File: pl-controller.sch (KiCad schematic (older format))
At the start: 31 parts

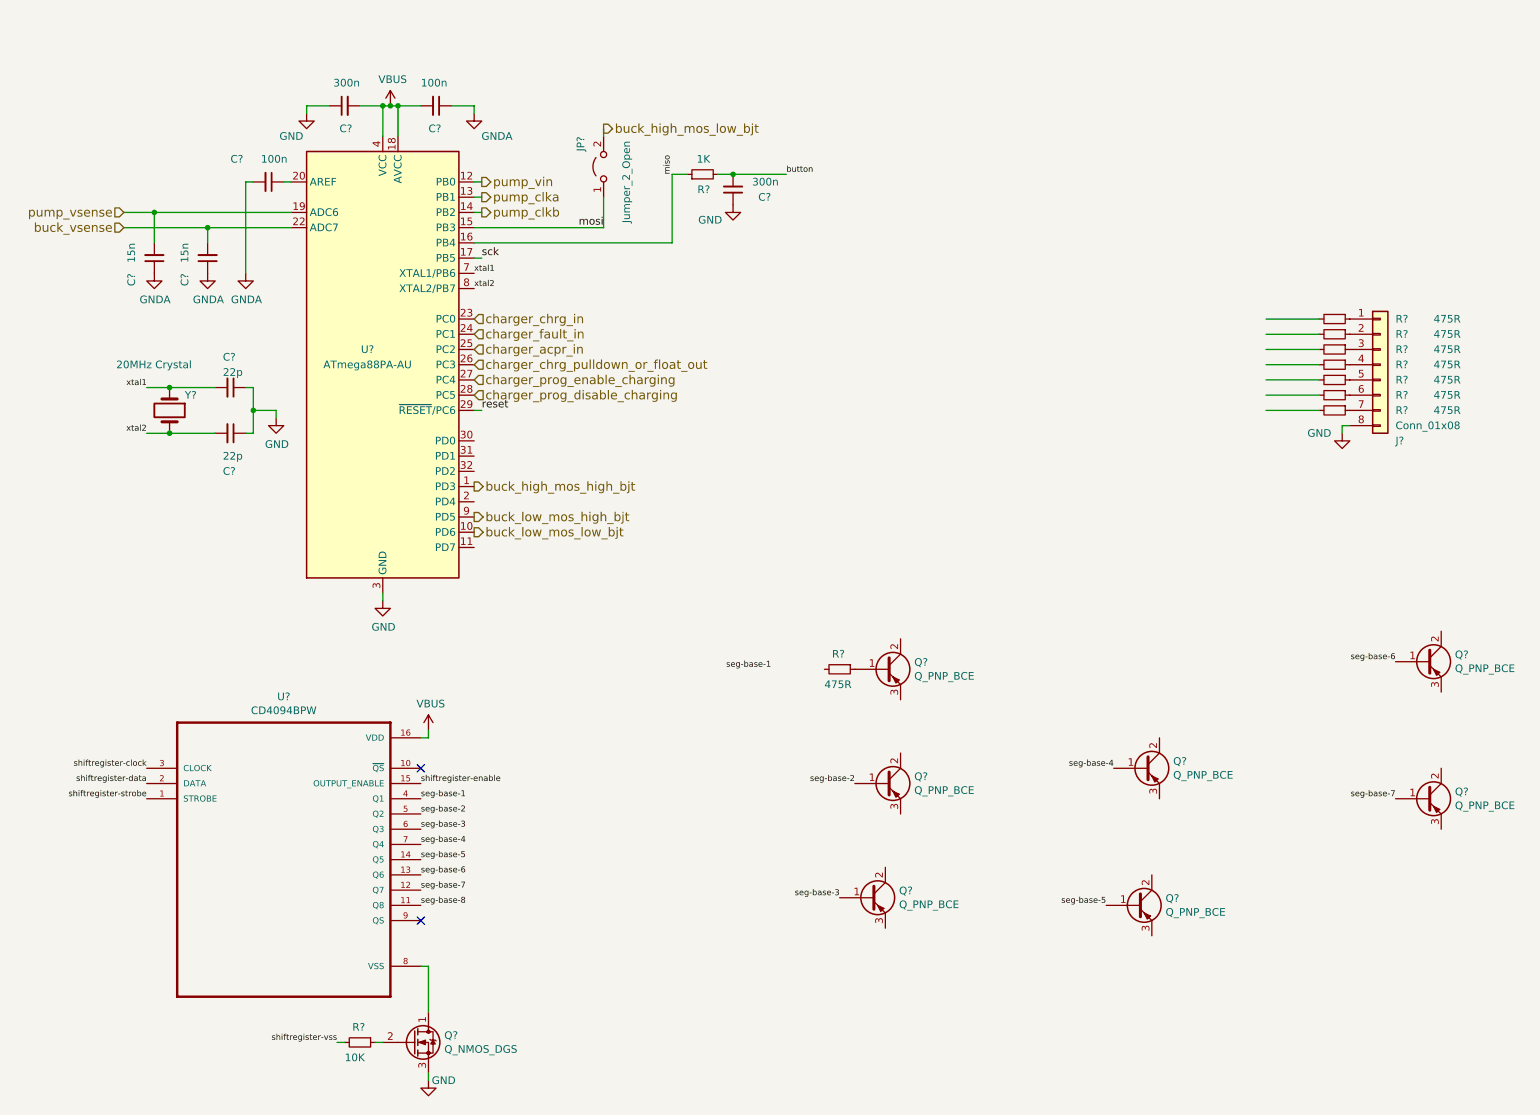
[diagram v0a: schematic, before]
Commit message: Added component values
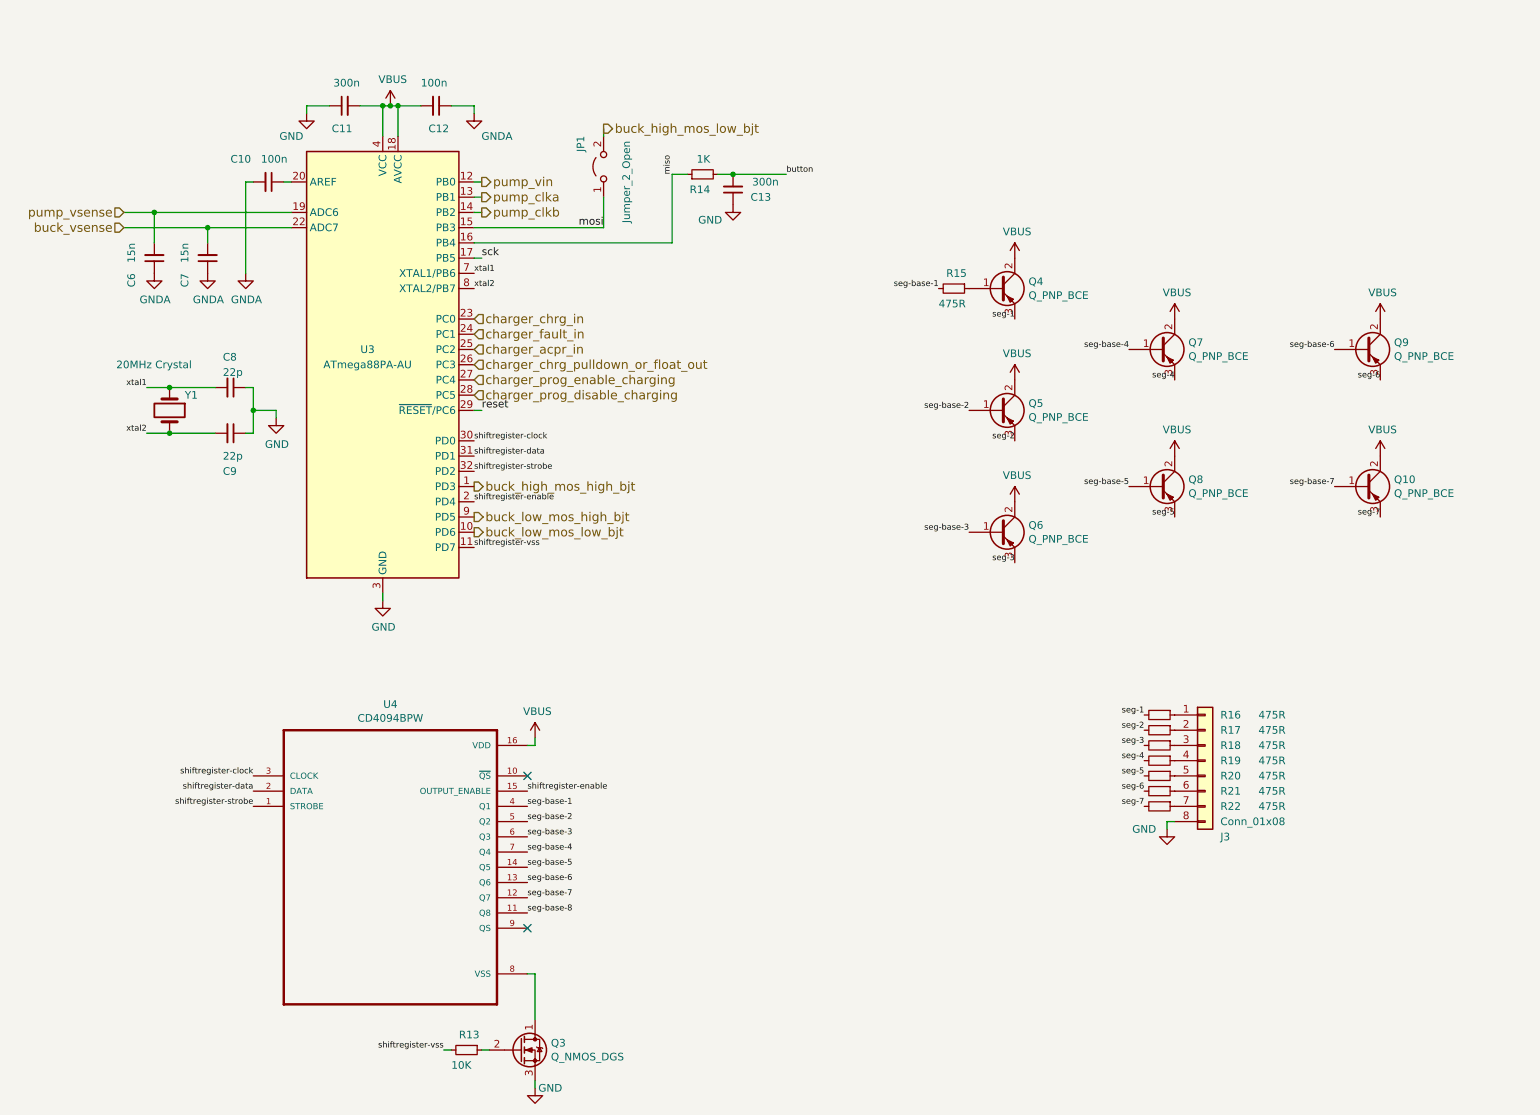
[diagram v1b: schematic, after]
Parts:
- gave numbers to parts that had none: 31
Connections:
- net labels added: seg-1, seg-2, seg-3, seg-4, seg-5, seg-6, seg-7
- wire segments 59 -> 52
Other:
- moved on the sheet: J3, Q10, Q3, Q4, Q5, Q6, Q7, Q8, Q9, R13, R15, R16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

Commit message: Schematics redesigned and fixed
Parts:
- added C10: 300n, Capacitor_SMD:C_0805_2012Metric_Pad1.15x1.40mm_HandSolder, symbol portable-light-rescue:C_Small-Device
- added C14, C15: 100n, Capacitor_SMD:C_1206_3216Metric_Pad1.42x1.75mm_HandSolder, symbol portable-light-rescue:C_Small-Device
- added D1: M7, Diode_SMD:D_SMA_Handsoldering, symbol Device:D_Small
- added D2, D3: 1N5819, Diode_SMD:D_SMA_Handsoldering, symbol portable-light-rescue:1N5819-Diode
- added J11: Conn_01x05, Connector_PinHeader_2.54mm:PinHeader_1x05_P2.54mm_Vertical, symbol Connector_Generic:Conn_01x05
- added R23, R24, R25, R26, R27, R28: 5K1, Capacitor_SMD:C_0805_2012Metric_Pad1.15x1.40mm_HandSolder, symbol portable-light-rescue:R_Small-Device
- added U4: L78L05_SOT89, Package_TO_SOT_SMD:SOT-89-3, symbol portable-light-rescue:L78L05_SOT89-Regulator_Linear
- C11: value 300n -> 100n; footprint Capacitor_SMD:C_0805_2012Metric_Pad1.15x1.40mm_HandSolder -> Capacitor_SMD:C_1206_3216Metric_Pad1.42x1.75mm_HandSolder
- J12: renamed from J3; footprint (none) -> Ribbon_Cable:Ribbon_8
- JP1: value Jumper_2_Open -> Jumper_Mosfet_Open
- Q10: renamed from Q8; footprint (none) -> Package_TO_SOT_SMD:SOT-23
- Q3, Q4, Q5, Q6, Q9: footprint (none) -> Package_TO_SOT_SMD:SOT-23
- Q7: renamed from Q10; footprint (none) -> Package_TO_SOT_SMD:SOT-23
- Q8: renamed from Q7; footprint (none) -> Package_TO_SOT_SMD:SOT-23
- R22: renamed from R15; value 475R -> 5K1; footprint Resistor_SMD:R_1206_3216Metric_Pad1.42x1.75mm_HandSolder -> Capacitor_SMD:C_0805_2012Metric_Pad1.15x1.40mm_HandSolder
- U3: renamed from U4; footprint SOP-16_4.55x10.3mm_P1.27mm -> UniX_Generic:SOP-16
- renumbered C6 to C5, C7 to C6, C8 to C7, C9 to C8, C10 to C9, R16 to R15, R17 to R16, R18 to R17, R19 to R18, R20 to R19, R21 to R20, R22 to R21, U3 to U2
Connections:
- net labels added: +5V, +BATT-1, +PUMP-2, pump_onoff
- net labels removed: GNDA, VBUS, pump_vin, seg-base-8
- wire segments 52 -> 84
- no-connect marks 2 -> 3
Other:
- moved on the sheet: C11, J12, Q10, Q4, Q5, Q6, Q7, Q8, Q9, R15, R16, R17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

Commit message: Cleaned up the PCB a little bit, Fixed some errors in schematics
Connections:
- net labels added: +BATT-2
- net labels removed: +BATT-1
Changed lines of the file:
@@
 $EndComp
 Text GLabel 9750 2050 1    39   UnSpc ~ 0
-+BATT-1
++BATT-2
 Wire Wire Line
 	9750 2050 9750 2550

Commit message: Fixed some minor stuff in schematics, Refined the PCB a little bit more
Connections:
- net labels added: GNDA
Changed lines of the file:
@@
 Wire Wire Line
 	4000 6850 4000 6700
-Text Label 7350 4250 2    39   ~ 0
+Text Label 8400 4650 2    39   ~ 0
 seg-base-1
 Wire Wire Line
@@
 Text Label 9400 5050 2    39   ~ 0
 seg-base-6
-Text Label 8350 5450 2    39   ~ 0
+Text Label 9400 5850 2    39   ~ 0
 seg-base-5
-Text Label 8400 4650 2    39   ~ 0
+Text Label 7350 4250 2    39   ~ 0
 seg-base-4
-Text Label 7350 5050 2    39   ~ 0
+Text Label 7350 5850 2    39   ~ 0
 seg-base-2
 $Comp
@@
 	0    1    1    0
 $EndComp
-Text Label 9400 5850 2    39   ~ 0
+Text Label 8350 5450 2    39   ~ 0
 seg-base-7
 $Comp
@@
 	0    1    1    0
 $EndComp
-Text Label 7350 5850 2    39   ~ 0
+Text Label 7350 5050 2    39   ~ 0
 seg-base-3
 $Comp
@@
 	0    1    1    0
 $EndComp
-Text Label 5350 7050 2    39   ~ 0
-seg-7
-Text Label 5350 6850 2    39   ~ 0
-seg-5
 $Comp
 L Device:Q_PNP_BCE Q10
@@
 	1    9500 5850
 	0    1    1    0
-$EndComp
-$Comp
-L portable-light-rescue:GND-power #PWR015
-U 1 1 5F6B2439
-P 3600 900
-F 0 "#PWR015" H 3600 650 50  0001 C CNN
-F 1 "GND" H 3700 750 50  0000 C CNN
-F 2 "" H 3600 900 50  0001 C CNN
-F 3 "" H 3600 900 50  0001 C CNN
-	1    3600 900
-	1    0    0    -1
-$EndComp
-$Comp
-L power:GND #PWR011
-U 1 1 5F66406C
-P 2100 1950
-F 0 "#PWR011" H 2100 1700 50  0001 C CNN
-F 1 "GND" H 2105 1777 50  0000 C CNN
-F 2 "" H 2100 1950 50  0001 C CNN
-F 3 "" H 2100 1950 50  0001 C CNN
-	1    2100 1950
-	1    0    0    -1
 $EndComp
 $Comp
@@
 	1    0    0    -1
 $EndComp
+Text Label 5350 7050 2    39   ~ 0
+seg-7
+Text Label 5350 6850 2    39   ~ 0
+seg-5
+$Comp
+L power:GNDA #PWR?
+U 1 1 5F74E657
+P 3600 900
+F 0 "#PWR?" H 3600 650 50  0001 C CNN
+F 1 "GNDA" H 3605 727 50  0000 C CNN
+F 2 "" H 3600 900 50  0001 C CNN
+F 3 "" H 3600 900 50  0001 C CNN
+	1    3600 900
+	1    0    0    -1
+$EndComp
+$Comp
+L power:GNDA #PWR?
+U 1 1 5F7553B9
+P 2100 1950
+F 0 "#PWR?" H 2100 1700 50  0001 C CNN
+F 1 "GNDA" H 2105 1777 50  0000 C CNN
+F 2 "" H 2100 1950 50  0001 C CNN
+F 3 "" H 2100 1950 50  0001 C CNN
+	1    2100 1950
+	1    0    0    -1
+$EndComp

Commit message: Seperated the two PCBs successfully, All DRC errors fixed, gotta double check the circuit
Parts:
- removed JP1: Jumper_Mosfet_Open, Jumper:SolderJumper-2_P1.3mm_Open_RoundedPad1.0x1.5mm, symbol portable-light-rescue:Jumper_2_Open-Jumper
- added J13: Conn_01x02-Connector_Generic, Ribbon_Cable:Ribbon_2, symbol portable-light-rescue:Conn_01x02-Connector_Generic
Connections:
- wire segments 84 -> 86
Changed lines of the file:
@@
 	2100 1350 2100 1950
 $Comp
-L portable-light-rescue:GND-power #PWR014
+L portable-light-rescue:GND-power #PWR012
 U 1 1 5F308B2E
 P 3000 4100
-F 0 "#PWR014" H 3000 3850 50  0001 C CNN
+F 0 "#PWR012" H 3000 3850 50  0001 C CNN
 F 1 "GND" H 3005 3927 50  0000 C CNN
 F 2 "" H 3000 4100 50  0001 C CNN
@@
 $EndComp
 $Comp
-L portable-light-rescue:GND-power #PWR012
+L portable-light-rescue:GND-power #PWR010
 U 1 1 5F54FF00
 P 2300 2900
-F 0 "#PWR012" H 2300 2650 50  0001 C CNN
+F 0 "#PWR010" H 2300 2650 50  0001 C CNN
 F 1 "GND" H 2305 2727 50  0000 C CNN
 F 2 "" H 2300 2900 50  0001 C CNN
@@
 $EndComp
 $Comp
-L portable-light-rescue:GND-power #PWR013
+L portable-light-rescue:GND-power #PWR011
 U 1 1 5F30EFD6
 P 2500 900
-F 0 "#PWR013" H 2500 650 50  0001 C CNN
+F 0 "#PWR011" H 2500 650 50  0001 C CNN
 F 1 "GND" H 2400 750 50  0000 C CNN
 F 2 "" H 2500 900 50  0001 C CNN
@@
 Wire Wire Line
 	3600 850  3600 900
-$Comp
-L portable-light-rescue:Jumper_2_Open-Jumper JP1
-U 1 1 5F316715
-P 4450 1250
-F 0 "JP1" H 4600 1400 50  0000 C CNN
-F 1 "Jumper_Mosfet_Open" H 4150 1100 50  0000 C CNN
-F 2 "Jumper:SolderJumper-2_P1.3mm_Open_RoundedPad1.0x1.5mm" H 4450 1250 50  0001 C CNN
-F 3 "~" H 4450 1250 50  0001 C CNN
-	1    4450 1250
-	0    -1   -1   0
-$EndComp
-Wire Wire Line
-	4450 1050 4450 1000
-Wire Wire Line
-	4450 1450 4450 1650
 Wire Wire Line
 	3600 1650 4450 1650
@@
 $EndComp
 $Comp
-L portable-light-rescue:GND-power #PWR018
+L portable-light-rescue:GND-power #PWR016
 U 1 1 5F5C8E7B
 P 5300 1500
-F 0 "#PWR018" H 5300 1250 50  0001 C CNN
+F 0 "#PWR016" H 5300 1250 50  0001 C CNN
 F 1 "GND" H 5150 1400 50  0000 C CNN
 F 2 "" H 5300 1500 50  0001 C CNN
@@
 $EndComp
 $Comp
-L portable-light-rescue:GND-power #PWR016
+L portable-light-rescue:GND-power #PWR014
 U 1 1 5F55F250
 P 4000 7300
-F 0 "#PWR016" H 4000 7050 50  0001 C CNN
+F 0 "#PWR014" H 4000 7050 50  0001 C CNN
 F 1 "GND" H 3900 7300 50  0000 C CNN
 F 2 "" H 4000 7300 50  0001 C CNN
@@
 $EndComp
 $Comp
-L portable-light-rescue:GND-power #PWR019
+L portable-light-rescue:GND-power #PWR017
 U 1 1 5F54FEFF
 P 5500 7200
-F 0 "#PWR019" H 5500 6950 50  0001 C CNN
+F 0 "#PWR017" H 5500 6950 50  0001 C CNN
 F 1 "GND" H 5650 7200 50  0000 C CNN
 F 2 "" H 5500 7200 50  0001 C CNN
@@
 $EndComp
 $Comp
-L portable-light-rescue:GND-power #PWR017
+L portable-light-rescue:GND-power #PWR015
 U 1 1 5F754173
 P 4850 4600
-F 0 "#PWR017" H 4850 4350 50  0001 C CNN
+F 0 "#PWR015" H 4850 4350 50  0001 C CNN
 F 1 "GND" H 5000 4600 50  0000 C CNN
 F 2 "" H 4850 4600 50  0001 C CNN
@@
 	1    9500 5850
 	0    1    1    0
-$EndComp
-$Comp
-L power:GND #PWR010
-U 1 1 5F66442A
-P 1850 1950
-F 0 "#PWR010" H 1850 1700 50  0001 C CNN
-F 1 "GND" H 1855 1777 50  0000 C CNN
-F 2 "" H 1850 1950 50  0001 C CNN
-F 3 "" H 1850 1950 50  0001 C CNN
-	1    1850 1950
-	1    0    0    -1
-$EndComp
-$Comp
-L power:GND #PWR09
-U 1 1 5F664659
-P 1500 1950
-F 0 "#PWR09" H 1500 1700 50  0001 C CNN
-F 1 "GND" H 1505 1777 50  0000 C CNN
-F 2 "" H 1500 1950 50  0001 C CNN
-F 3 "" H 1500 1950 50  0001 C CNN
-	1    1500 1950
-	1    0    0    -1
 $EndComp
 Text GLabel 3050 700  1    79   UnSpc ~ 0
@@
 	9400 2000 9400 2900
 $Comp
-L power:PWR_FLAG #FLG09
+L power:PWR_FLAG #FLG010
 U 1 1 5F892826
 P 9400 2000
-AR Path="/5F378869/5F892826" Ref="#FLG09"  Part="1"
+AR Path="/5F378869/5F892826" Ref="#FLG010"  Part="1"
 AR Path="/5F892826" Ref="#FLG?"  Part="1"
-F 0 "#FLG09" H 9400 2075 50  0001 C CNN
+F 0 "#FLG010" H 9400 2075 50  0001 C CNN
 F 1 "PWR_FLAG" V 9400 2128 50  0000 L CNN
 F 2 "" H 9400 2000 50  0001 C CNN
@@
 	7800 2200 7800 2450
 $Comp
-L power:PWR_FLAG #FLG08
+L power:PWR_FLAG #FLG09
 U 1 1 5F988FD1
 P 4000 6700
-F 0 "#FLG08" H 4000 6775 50  0001 C CNN
+F 0 "#FLG09" H 4000 6775 50  0001 C CNN
 F 1 "PWR_FLAG" V 4000 6828 50  0000 L CNN
 F 2 "" H 4000 6700 50  0001 C CNN
@@
 	8350 2750 8350 2850
 $Comp
-L power:GND #PWR020
+L power:GND #PWR019
 U 1 1 5F99CBBF
 P 7950 2850
-F 0 "#PWR020" H 7950 2600 50  0001 C CNN
+F 0 "#PWR019" H 7950 2600 50  0001 C CNN
 F 1 "GND" H 7955 2677 50  0000 C CNN
 F 2 "" H 7950 2850 50  0001 C CNN
@@
 $EndComp
 $Comp
-L power:GND #PWR021
+L power:GND #PWR020
 U 1 1 5F99D577
 P 8350 2850
-F 0 "#PWR021" H 8350 2600 50  0001 C CNN
+F 0 "#PWR020" H 8350 2600 50  0001 C CNN
 F 1 "GND" H 8355 2677 50  0000 C CNN
 F 2 "" H 8350 2850 50  0001 C CNN
@@
 $EndComp
 $Comp
-L power:GND #PWR022
+L power:GND #PWR021
 U 1 1 5F99D9B7
 P 8750 2850
-F 0 "#PWR022" H 8750 2600 50  0001 C CNN
+F 0 "#PWR021" H 8750 2600 50  0001 C CNN
 F 1 "GND" H 8755 2677 50  0000 C CNN
 F 2 "" H 8750 2850 50  0001 C CNN
@@
 seg-5
 $Comp
-L power:GNDA #PWR?
+L power:GNDA #PWR013
 U 1 1 5F74E657
 P 3600 900
-F 0 "#PWR?" H 3600 650 50  0001 C CNN
+F 0 "#PWR013" H 3600 650 50  0001 C CNN
 F 1 "GNDA" H 3605 727 50  0000 C CNN
 F 2 "" H 3600 900 50  0001 C CNN
@@
 $EndComp
 $Comp
-L power:GNDA #PWR?
+L power:GNDA #PWR09
 U 1 1 5F7553B9
 P 2100 1950
-F 0 "#PWR?" H 2100 1700 50  0001 C CNN
+F 0 "#PWR09" H 2100 1700 50  0001 C CNN
 F 1 "GNDA" H 2105 1777 50  0000 C CNN
 F 2 "" H 2100 1950 50  0001 C CNN
@@
 	1    0    0    -1
 $EndComp
+$Comp
+L power:GNDA #PWR08
+U 1 1 5F72CF02
+P 1850 1950
+F 0 "#PWR08" H 1850 1700 50  0001 C CNN
+F 1 "GNDA" H 1855 1777 50  0000 C CNN
+F 2 "" H 1850 1950 50  0001 C CNN
+F 3 "" H 1850 1950 50  0001 C CNN
+	1    1850 1950
+	1    0    0    -1
+$EndComp
+$Comp
+L power:GNDA #PWR07
+U 1 1 5F72D104
+P 1500 1950
+F 0 "#PWR07" H 1500 1700 50  0001 C CNN
+F 1 "GNDA" H 1505 1777 50  0000 C CNN
+F 2 "" H 1500 1950 50  0001 C CNN
+F 3 "" H 1500 1950 50  0001 C CNN
+	1    1500 1950
+	1    0    0    -1
+$EndComp
+$Comp
+L portable-light-rescue:Conn_01x02-Connector_Generic J13
+U 1 1 5F7B8BB3
+P 5800 1950
+F 0 "J13" H 5880 1942 50  0000 L CNN
+F 1 "Conn_01x02-Connector_Generic" H 5880 1851 50  0000 L CNN
+F 2 "Ribbon_Cable:Ribbon_2" H 5800 1950 50  0001 C CNN
+F 3 "" H 5800 1950 50  0001 C CNN
+	1    5800 1950
+	1    0    0    -1
+$EndComp
+$Comp
+L portable-light-rescue:GND-power #PWR018
+U 1 1 5F7BD62C
+P 5550 2100
+F 0 "#PWR018" H 5550 1850 50  0001 C CNN
+F 1 "GND" H 5400 2000 50  0000 C CNN
+F 2 "" H 5550 2100 50  0001 C CNN
+F 3 "" H 5550 2100 50  0001 C CNN
+	1    5550 2100
+	1    0    0    -1
+$EndComp
+Wire Wire Line
+	5550 2100 5550 2050
+Wire Wire Line
+	5550 2050 5600 2050
+Text Label 5550 1950 2    39   ~ 0
+button
+Wire Wire Line
+	5550 1950 5600 1950
+Wire Wire Line
+	4450 1000 4450 1650
 $EndSCHEMATC
